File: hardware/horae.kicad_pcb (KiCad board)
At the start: 4 copper layers, 38.5 x 16.5 mm, 76 parts, among them J1 FH34SRJ-18S-0.5SH(50), Q1 AO3400A, Q2 CJ3134K, U1 ESP32-S3FN8, U2 TP4054, U3 RT9080-33, U4 USBLC6-2P6, U5 RV-3032-C7, U6 LIS2DUX12, Y1 40MHz 15pF

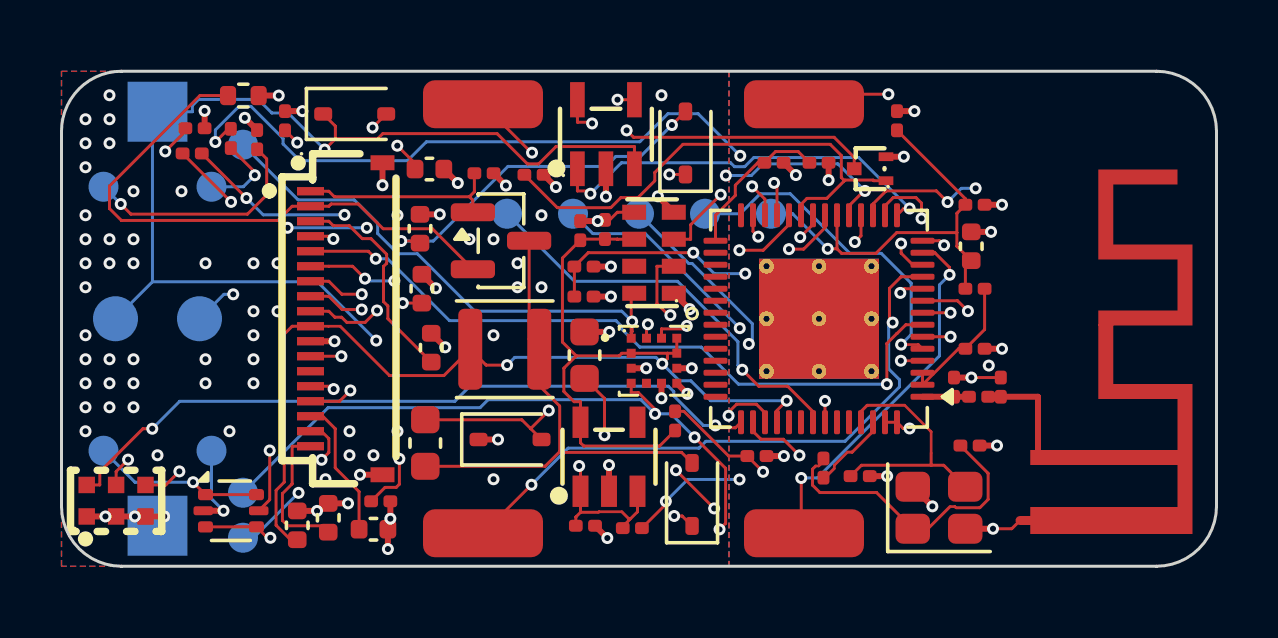
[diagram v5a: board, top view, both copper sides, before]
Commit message: Rev A slim: 33.8 x 16.2 x 0.6 mm board, case under a Charge 3 (35.6 x 18.0 x 7.05)
- Board: 16.2 mm wide (was 18.0), 2.8 mm antenna zone past the glass, 0.6 mm 4-layer;
  ERC 0, DRC 0 errors / 0 warnings / 0 unconnected, every signal routed on the first pass.
- Tallest part 1.0 mm (was 1.2): PMZ390UN MOSFETs (SOT-883), PMEG3005EL Schottkys
  (SOD-882), FNR3010 47 uH 3x3x1.0, 0402 4.7 uF/25 V; SSD1681 reference values.
- RTC IC dropped: 32.768 kHz crystal on GPIO15/16 runs the ESP32 RTC (Watchy v3 /
  Yatchy approach, -$3.44).
- Power: BQ25101 charger (75 nA drain, 28 V input, 24 mA for the 40-55 mAh cell) and
  TPS62840 buck (60 nA Iq, 267k VSET -> 3.3 V) replace TP4054 + RT9080; hand-placed buck cell.
- GPIO plan: display + I2C on the U1 side facing J1 (RTC GPIOs, ULP-drivable), touch /
  interrupts / haptics / ADC on the antenna side; USB straight to the ESP32.
- RF match from the openEMS re-run: C11 0.3 pF, L3 1.2 nH (C12 DNP).
- Fixes: C28 footprint/part mismatch (0201 pads, 0402 part); route.py took the first rule
  area as the antenna keep-out (pours on F/In2/B stopped at x = -7.5); RF shunt vias get
  their own stub; build.sh died on a perfect route (grep -c exit 1); broken EasyEDA pads
  on the 0603 inductor; silk moved to fab, battery +/- marks on the bottom.
- README: Standard PCBA is required (0201s, 0.4 mm WCSPs), corrected cost, real battery
  capacity (40-55 mAh), motor/battery soldered, review checklist, GPIO table. cost.py added.

Co-Authored-By: Claude Opus 5.5 <noreply@anthropic.com>
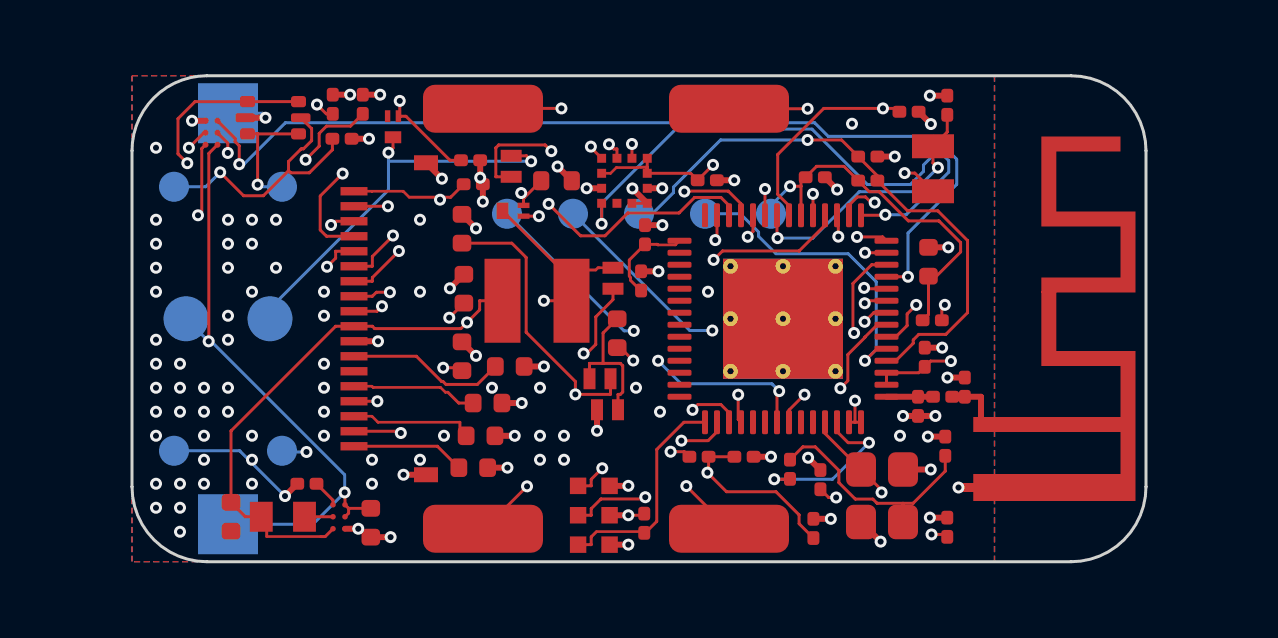
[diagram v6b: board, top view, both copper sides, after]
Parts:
- removed C16: 1uF, Capacitor_SMD:C_0201_0603Metric
- removed C19: 100nF, Capacitor_SMD:C_0201_0603Metric
- removed R7, R8: 22, Resistor_SMD:R_0201_0603Metric
- removed TP14: I2C_SDA, TestPoint:TestPoint_Pad_D1.0mm
- removed TP15: I2C_SCL, TestPoint:TestPoint_Pad_D1.0mm
- removed TP16: PPG_INT, TestPoint:TestPoint_Pad_D1.0mm
- removed U5: RV-3032-C7, horae:OSC-SMD_8P-L3.2-W1.5-P0.90-BL
- added C32: 20pF, Capacitor_SMD:C_0201_0603Metric, F.Cu at (109.0, 93.1)
- added C33: 20pF, Capacitor_SMD:C_0201_0603Metric, F.Cu at (110.3, 92.9)
- added L5: 2.2uH, horae:IND-SMD_L1.6-W0.8, F.Cu at (88.1, 106.6)
- added R5: 10k, Resistor_SMD:R_0201_0603Metric, F.Cu at (90.8, 92.9)
- added R6: 267k, Resistor_SMD:R_0201_0603Metric, F.Cu at (88.9, 105.5)
- added Y2: 32.768kHz 12.5pF, horae:CRYSTAL-SMD_L2.1-W1.2-P1.50, F.Cu at (109.8, 95.0)
- C11: value 0.9pF -> 0.3pF
- C15: value 22uF -> 10uF; footprint Capacitor_SMD:C_0603_1608Metric -> Capacitor_SMD:C_0402_1005Metric
- C22: footprint Capacitor_SMD:C_0603_1608Metric -> Capacitor_SMD:C_0402_1005Metric
- C28: footprint Capacitor_SMD:C_0201_0603Metric -> Capacitor_SMD:C_0402_1005Metric
- D1, D2, D3, D4: value B5819WS -> PMEG3005EL; footprint Diode_SMD:D_SOD-323 -> horae:SOD-882_L1.0-W0.6-RD
- L3: value 0.6nH -> 1.2nH
- L4: footprint Inductor_SMD:L_Sunlord_SWPA3012S -> horae:IND-SMD_L3.0-W3.0_FNR3010S
- Q1: value AO3400A -> PMZ390UN; footprint Package_TO_SOT_SMD:SOT-23 -> horae:SOT-883-3_L1.0-W0.6-BR
- Q2: value CJ3134K -> PMZ390UN; footprint horae:SOT-723_L1.2-W0.8-P0.40-LS1.2-BR -> horae:SOT-883-3_L1.0-W0.6-BR
- R2: value 20k -> 5.6k
- U2: value TP4054 -> BQ25101; footprint horae:SOT-23-5_L3.0-W1.7-P0.95-LS2.8-BL -> horae:DSBGA-6_L0.9-W1.6-R2-C3-P0.40-BL
- U3: value RT9080-33 -> TPS62840; footprint horae:TSOT-23-5_L2.9-W1.6-P0.95-LS2.8-BL -> horae:DSBGA-6_L1.4-W1.0-R2-C3-P0.40-BL
- moved C31 19.9 mm to (100.2, 106.8), turned to 90 degrees
- moved Q2 16.0 mm to (91.8, 93.6), turned to 90 degrees
- moved MIC1 15.9 mm to (98.5, 106.5), turned to 180 degrees
- moved TP5 13.9 mm to (86.3, 106.8)
- moved TP6 13.9 mm to (86.3, 93.2)
- moved U4 13.2 mm to (87.8, 93.3)
- moved U2 13.1 mm to (85.8, 93.8), turned to 90 degrees
- moved C18 11.6 mm to (105.8, 107.0), turned to 90 degrees
- moved R12 10.8 mm to (97.2, 95.4)
- moved C10 10.6 mm to (107.6, 94.6)
- moved C6 10.5 mm to (106.0, 105.4), turned to 90 degrees
- moved R1 10.3 mm to (107.6, 95.4), turned to 0 degrees
- moved U3 9.22 mm to (90.0, 106.6), turned to 90 degrees
- moved C15 9.05 mm to (91.1, 106.8), turned to -90 degrees
- moved D1 8.36 mm to (98.7, 102.0), turned to 0 degrees
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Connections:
- R2 pad 1: PROG -> CHG_ISET
- U1 pad 10: RTC_INT -> VIB
- U1 pad 11: TOUCH_BACK -> CHG_STAT
- U1 pad 12: TOUCH_MENU -> BAT_ADC
- U1 pad 13: TOUCH_DOWN -> ACC_INT2
- U1 pad 14: BAT_ADC -> ACC_INT1
- U1 pad 15: CHG_STAT -> I2C_SDA
- U1 pad 17: I2C_SDA -> EPD_BUSY
- U1 pad 18: EPD_MOSI -> EPD_RES
- U1 pad 19: PPG_INT -> EPD_DC
- U1 pad 21: EPD_DC -> XTAL32_P
- U1 pad 22: EPD_CS -> XTAL32_N
- U1 pad 23: VIB -> EPD_CS
- U1 pad 24: ACC_INT1 -> EPD_SCK
- U1 pad 25: ESP_DM -> USB_DM
- U1 pad 26: ESP_DP -> USB_DP
- U1 pad 27: ACC_INT2 -> EPD_MOSI
- U1 pad 6: EPD_BUSY -> TOUCH_DOWN
- U1 pad 7: EPD_RES -> TOUCH_BACK
- U1 pad 8: TOUCH_UP -> TOUCH_MENU
- U1 pad 9: EPD_SCK -> TOUCH_UP
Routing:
- net PPG_INT: track 33.4 -> 0.00 mm, vias 5 -> 0
- net I2C_SDA: track 50.1 -> 19.2 mm, vias 6 -> 2
- net VBUS: track 40.8 -> 13.3 mm, vias 3 -> 2
- net MIC_VDD: track 34.6 -> 7.52 mm, vias 3 -> 0
- net MIC_CLK: track 29.8 -> 5.82 mm
- net ESP_DM: track 23.6 -> 0.00 mm, vias 3 -> 0
- net USB_DP: track 17.9 -> 41.3 mm, vias 2 -> 3
- net ESP_DP: track 21.6 -> 0.00 mm, vias 3 -> 0
- net I2C_SCL: track 32.8 -> 13.1 mm
- net MIC_DATA: track 27.0 -> 7.90 mm
- net CHG_STAT: track 13.7 -> 32.0 mm
- net EPD_SCK: track 32.4 -> 14.9 mm, vias 4 -> 2
- net RTC_INT: track 17.0 -> 0.00 mm, vias 2 -> 0
- net MOT_N: track 26.6 -> 13.3 mm, vias 3 -> 2
- net EPD_MOSI: track 27.0 -> 13.9 mm
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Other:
- board size 38.5 x 16.5 mm -> 33.8 x 16.2 mm
- board text added: "+"
- board text added: "-"

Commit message: Rev A: C11 0.5 pF (RF v3); README for the 6.80 mm two-shell case and magnetic cable
ERC 0, DRC 0 errors / 0 warnings / 0 unconnected.

Co-Authored-By: Claude Opus 5.5 <noreply@anthropic.com>
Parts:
- C11: value 0.3pF -> 0.5pF

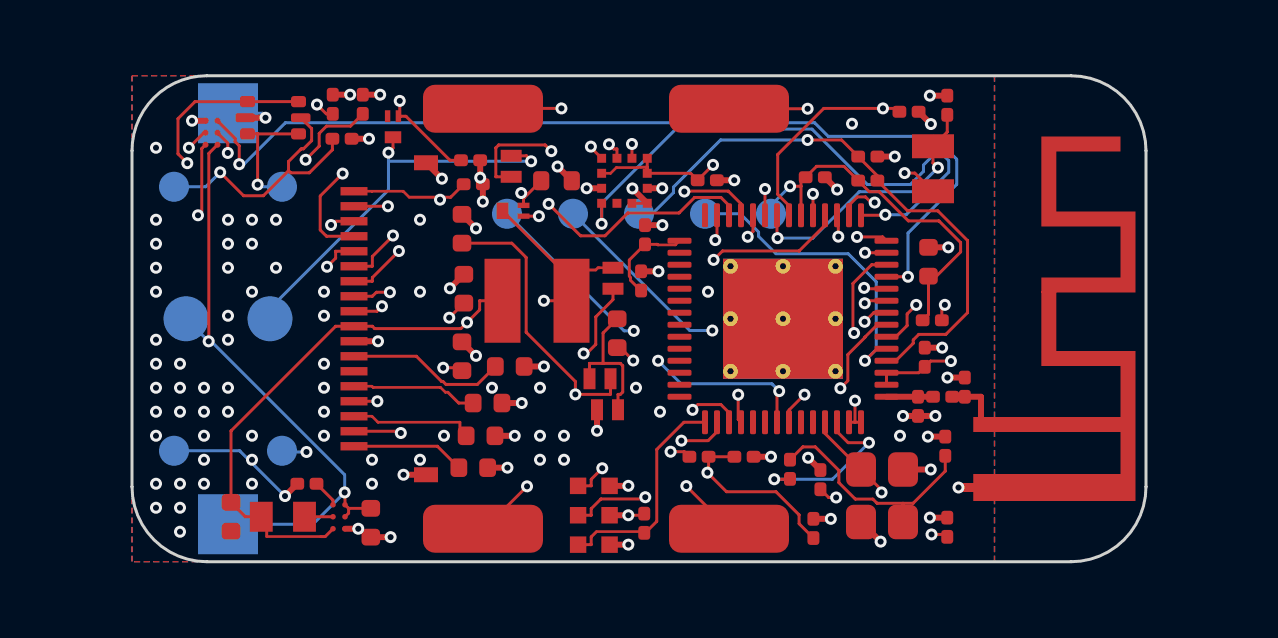
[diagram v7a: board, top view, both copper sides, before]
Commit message: Pre-order review: board, case and RF reworked; order and assembly guides
Four parallel reviews (schematic/parts, layout/fab, size, sourcing) found
7 blockers, all fixed:
- J1 faced the wrong way (FH34SRJ slot is on the fitting-nail side):
  turned, pins remapped (pad = 19 - display pin), moved +1.7 mm so the
  11.18 mm tail keeps GD's R > 0.5 bend
- CPL now in the gerber frame with JLC rotation offsets (U4, L4)
- TI's 0.23 mm NSMD lands for the BQ25101/TPS62840 WCSPs
- no foreign traces under the touch electrodes (all layers), 510R series
- RF match pads 0.15 mm apart, no paste on C12/AE1
- ESP32 EP per Espressif: vias in the mask webs, none in the paste
- 1-up 70 x 70 mm panel frame (panel.py) for JLC Standard PCBA

Also:
- 0.45/0.2 vias, power classes, decoupling at the pins, crystals on F.Cu,
  USB ESD flow-through, mic DATA/VDD swapped off the ROM-driven pin
- parts: LSCND1608 buck L (1.3 A), PMEG3002AEL, 2.2 uF rail caps, ST
  USBLC6, ISET RC, charger and booster input caps, KYX 40 MHz + 18 pF caps
- I2C on GPIO8/9 and INT on GPIO10/11; LIS2DUX12 now at 0x19
- PCB 33.6 x 16.0 (0.2 mm off every wall in the same case); six crush ribs
- RF v4 on the new layout: L3 1.2 -> 0.8 nH (worst in-band loss 0.78 dB)
- case: FPC loop model per GD, raised hood, ePTFE vent seat, TPU 90A only,
  cell max size, watertight exports, dock wiring diagram
- cost.py on JLC's current Standard fees ($1.53 per line, fixtures, X-ray)
- ORDER.md, ASSEMBLY.md, hardware README rewritten; timeline entry

ERC 0, DRC 0/0/0, JLC capability probe clean, reproducible build.

Co-Authored-By: Claude Opus 5.5 <noreply@anthropic.com>
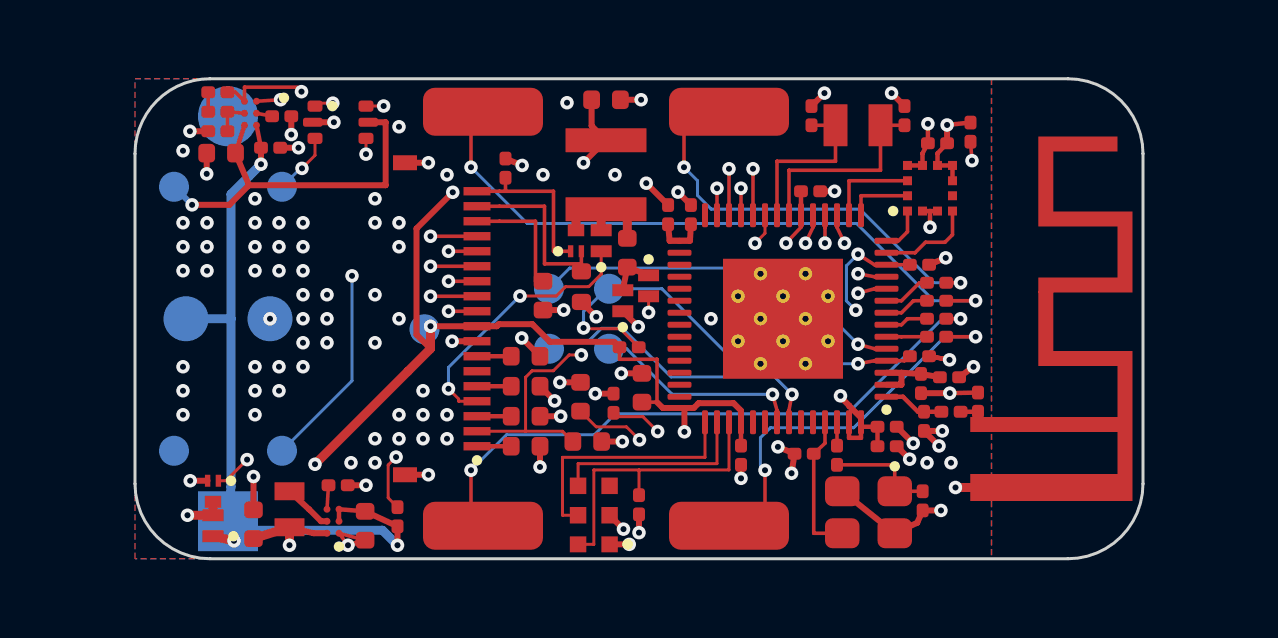
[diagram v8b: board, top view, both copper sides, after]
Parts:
- added C14: 1uF, Capacitor_SMD:C_0201_0603Metric, F.Cu at (87.7, 94.3)
- added C19: 10nF, Capacitor_SMD:C_0201_0603Metric, F.Cu at (86.0, 92.5)
- added C34: 100nF, Capacitor_SMD:C_0201_0603Metric, F.Cu at (103.4, 104.5)
- added C35: 10uF, Capacitor_SMD:C_0402_1005Metric, F.Cu at (98.9, 92.7)
- added C36: 10nF, Capacitor_SMD:C_0201_0603Metric, F.Cu at (108.3, 104.2)
- added R14: 510, Resistor_SMD:R_0201_0603Metric, F.Cu at (109.9, 98.8)
- added R15: 510, Resistor_SMD:R_0201_0603Metric, F.Cu at (109.9, 100.6)
- added R16: 510, Resistor_SMD:R_0201_0603Metric, F.Cu at (109.9, 99.4)
- added R17: 510, Resistor_SMD:R_0201_0603Metric, F.Cu at (109.9, 100.0)
- added R7: 2.7k, Resistor_SMD:R_0201_0603Metric, F.Cu at (86.0, 93.1)
- C1, C2: value 24pF -> 18pF
- C13: value 1uF -> 4.7uF/25V; footprint Capacitor_SMD:C_0201_0603Metric -> Capacitor_SMD:C_0402_1005Metric
- C24, C25, C28, C29: value 1uF/25V -> 2.2uF/25V
- C32, C33: value 20pF -> 18pF
- C6: value 100nF -> 1uF
- D1, D2, D3, D4: value PMEG3005EL -> PMEG3002AEL
- L3: value 1.2nH -> 0.8nH
- L4: footprint horae:IND-SMD_L3.0-W3.0_FNR3010S -> horae:IND-SMD_L3.0-W3.0_SWPA3010S
- R2: value 5.6k -> 6.8k
- TCH1: value TOUCH_UP -> TOUCH_UP_E
- TCH2: value TOUCH_DOWN -> TOUCH_DOWN_E
- TCH3: value TOUCH_MENU -> TOUCH_MENU_E
- TCH4: value TOUCH_BACK -> TOUCH_BACK_E
- TP2: value USB_DM -> USB_DM_POGO
- TP3: value USB_DP -> USB_DP_POGO
- TP6: footprint TestPoint:TestPoint_Pad_2.0x2.0mm -> TestPoint:TestPoint_Pad_D2.0mm
- U1: footprint Package_DFN_QFN:QFN-56-1EP_7x7mm_P0.4mm_EP4x4mm_ThermalVias -> horae:QFN-56-1EP_7x7mm_P0.4mm_EP4x4mm_Espressif
- Y1: value 40MHz 15pF -> 40MHz 12pF
- moved R13 16.7 mm to (111.0, 93.8), turned to 90 degrees
- moved D4 15.6 mm to (85.8, 106.9)
- moved Q2 13.6 mm to (85.8, 105.8)
- moved TP13 12.2 mm to (92.8, 100.3)
- moved C5 10.4 mm to (100.1, 102.3)
- moved R3 10.2 mm to (92.0, 106.6), turned to 90 degrees
- moved U6 10.2 mm to (109.7, 95.7), turned to 90 degrees
- moved R1 9.70 mm to (99.7, 101.0)
- moved C18 9.47 mm to (109.3, 98.2), turned to 0 degrees
- moved C24 8.23 mm to (98.3, 104.1), turned to 0 degrees
- moved C7 7.77 mm to (110.0, 94.2)
- moved C10 6.88 mm to (109.3, 101.2)
- moved TP12 5.77 mm to (97.0, 99.0)
- moved TP9 5.64 mm to (99.0, 101.0)
- moved C2 5.36 mm to (105.5, 104.5), turned to 180 degrees
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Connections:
- J1 pad 1: EPD_GDR -> EPD_VCOM
- J1 pad 10: +3V3 -> EPD_MOSI
- J1 pad 11: GND -> EPD_SCK
- J1 pad 12: EPD_VDD -> EPD_CS
- J1 pad 13: (no net) -> EPD_DC
- J1 pad 14: EPD_VSH1 -> EPD_RES
- J1 pad 15: PREVGH -> EPD_BUSY
- J1 pad 16: EPD_VSL -> EPD_VSHR
- J1 pad 17: PREVGL -> EPD_RESE
- J1 pad 18: EPD_VCOM -> EPD_GDR
- J1 pad 2: EPD_RESE -> PREVGL
- J1 pad 3: EPD_VSHR -> EPD_VSL
- J1 pad 4: EPD_BUSY -> PREVGH
- J1 pad 5: EPD_RES -> EPD_VSH1
- J1 pad 6: EPD_DC -> (no net)
- J1 pad 7: EPD_CS -> EPD_VDD
- J1 pad 8: EPD_SCK -> GND
- J1 pad 9: EPD_MOSI -> +3V3
- TCH1 pad 1: TOUCH_UP -> TOUCH_UP_E
- TCH2 pad 1: TOUCH_DOWN -> TOUCH_DOWN_E
- TCH3 pad 1: TOUCH_MENU -> TOUCH_MENU_E
- TCH4 pad 1: TOUCH_BACK -> TOUCH_BACK_E
- TP2 pad 1: USB_DM -> USB_DM_POGO
- TP3 pad 1: USB_DP -> USB_DP_POGO
- U1 pad 13: ACC_INT2 -> I2C_SDA
- U1 pad 14: ACC_INT1 -> I2C_SCL
- U1 pad 15: I2C_SDA -> ACC_INT1
- U1 pad 16: I2C_SCL -> ACC_INT2
- U1 pad 43: MIC_VDD -> MIC_DATA
- U1 pad 45: MIC_DATA -> MIC_VDD
- U4 pad 1: USB_DP -> USB_DP_POGO
- U4 pad 3: USB_DM -> USB_DM_POGO
- U6 pad 3: GND -> +3V3
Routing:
- net VBAT: track 51.1 -> 25.5 mm, vias 4 -> 3
- net USB_DP: track 41.3 -> 16.2 mm, vias 3 -> 2
- net TOUCH_MENU: track 23.5 -> 1.52 mm, vias 2 -> 0
- net TOUCH_MENU_E: track 0.00 -> 21.9 mm, vias 0 -> 2
- net TOUCH_BACK_E: track 0.00 -> 21.1 mm, vias 0 -> 2
- net TOUCH_DOWN: track 18.3 -> 1.35 mm, vias 2 -> 0
- net +3V3: track 69.3 -> 85.8 mm, vias 6 -> 11
- net I2C_SDA: track 19.2 -> 3.24 mm, vias 2 -> 0
- net TOUCH_BACK: track 17.0 -> 1.43 mm, vias 2 -> 0
- net TOUCH_UP_E: track 0.00 -> 14.9 mm, vias 0 -> 2
- net TOUCH_DOWN_E: track 0.00 -> 13.7 mm, vias 0 -> 2
- net USB_DP_POGO: track 0.00 -> 13.5 mm, vias 0 -> 2
- net I2C_SCL: track 13.1 -> 1.51 mm, vias 2 -> 0
- net EPD_RES: track 25.6 -> 15.0 mm
- net TOUCH_UP: track 12.0 -> 1.60 mm, vias 2 -> 0
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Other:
- board size 33.8 x 16.2 mm -> 33.6 x 16 mm
